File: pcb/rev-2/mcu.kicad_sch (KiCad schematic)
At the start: 8 parts, among them J5 BD125-10-A-0305-0580-L-B, U7 WT02C40C-V3

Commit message: pcb: full rev-2 layout
Mostly finished layout for the rev-2 board
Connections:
- net RAM.MISO: now also U7.A5 (P100); no longer U7.E6 (P010)
- net RAM.MOSI: now also U7.A1 (P006); no longer U7.11 (P009/BUTTON)
- net RAM.SCK: now also U7.A2 (P007); no longer U7.A3 (P008)
- net RAM.~{CS}: now also U7.A6 (P108); no longer JP4.2 (C)
- net SD.MISO: now also U7.E6 (P010); no longer U7.A5 (P100)
- net SD.MOSI: now also U7.11 (P009/BUTTON); no longer U7.A6 (P108)
- net SD.SCK: now also U7.A3 (P008); no longer U7.Z5 (P114)
- net SD.~{CS}: now also JP4.2 (C); no longer U7.Z6 (P115)
- net BUCKEN: now reaches R12.1, U7.B5 (P012)
- net IOVDD_CTRL: now reaches R13.1, U7.C1 (P031)
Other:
- moved on the sheet: R12, R13

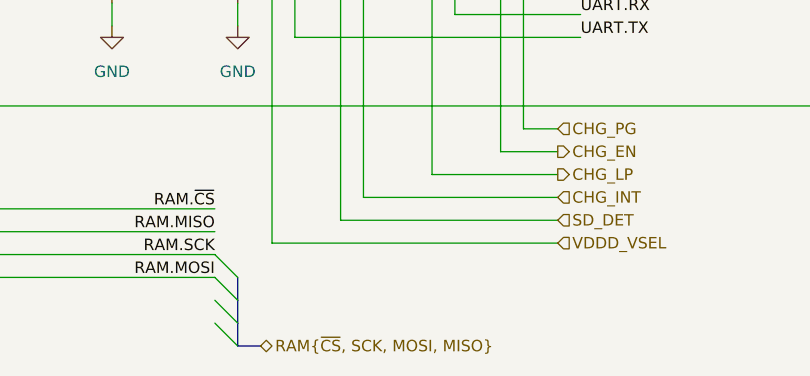
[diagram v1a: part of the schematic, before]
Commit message: pcb: minor schematic cleanup
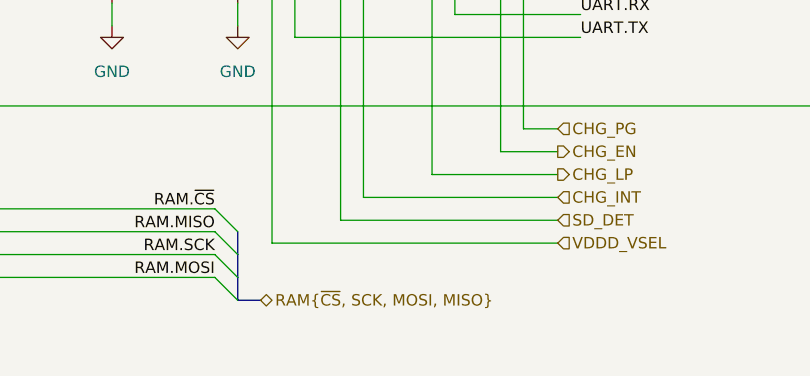
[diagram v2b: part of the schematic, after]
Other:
- title: (none) -> nRF53 Microcontroller

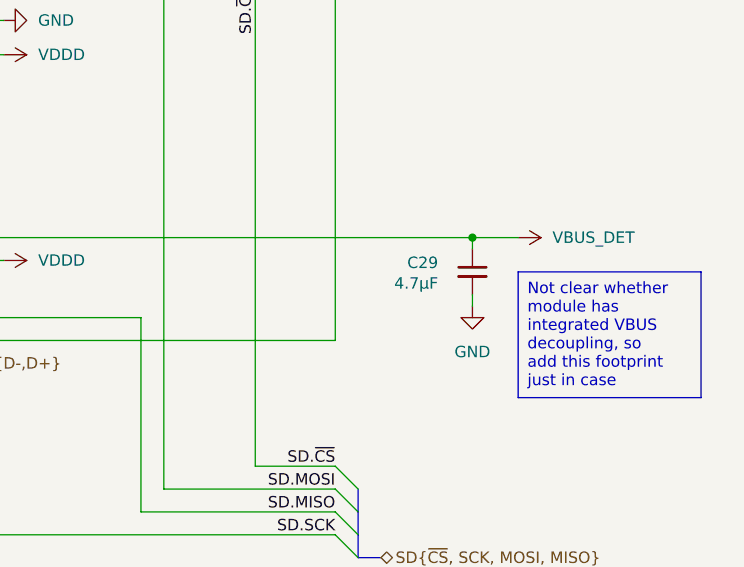
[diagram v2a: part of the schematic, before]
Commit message: pcb: update
Mostly downsize several decoupling capacitors to save space
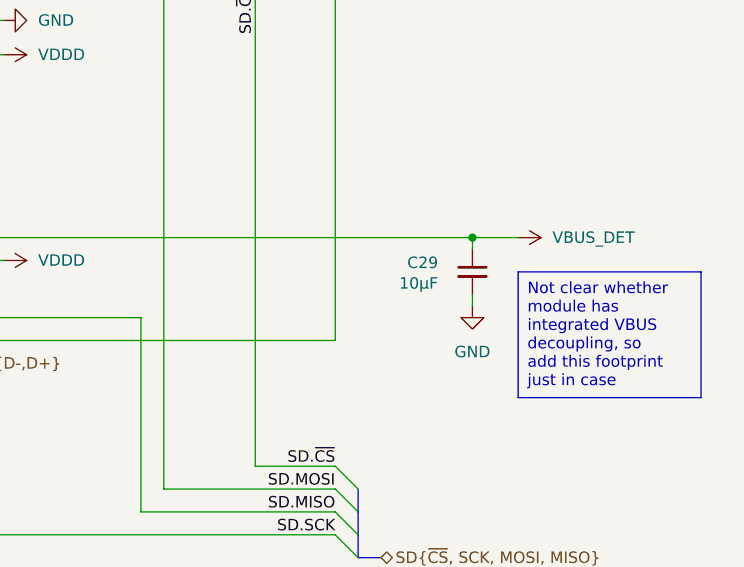
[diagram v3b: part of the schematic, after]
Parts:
- C29: value 4.7µF -> 10µF; footprint Capacitor_SMD:C_0603_1608Metric -> zeus-le:C_0402_1005Metric_Silkscreen_Clearance; manf# C1608X5R1E475K080AC -> CL05A106MP6NUN8
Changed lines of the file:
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@@
 			)
 		)
-		(property "Value" "4.7µF"
+		(property "Value" "10µF"
 			(at 254 110.4899 0)
 			(effects
@@
 			)
 		)
-		(property "Footprint" "Capacitor_SMD:C_0603_1608Metric"
+		(property "Footprint" "zeus-le:C_0402_1005Metric_Silkscreen_Clearance"
 			(at 257.81 109.22 0)
 			(effects
@@
 			)
 		)
-		(property "Description" "Capacitor, decoupling"
+		(property "Description" "Capacitor, decoupling, 10V, X5R"
 			(at 257.81 109.22 0)
 			(effects
@@
 			)
 		)
-		(property "manf#" "C1608X5R1E475K080AC"
+		(property "manf#" "CL05A106MP6NUN8"
 			(at 257.81 109.22 0)
 			(effects

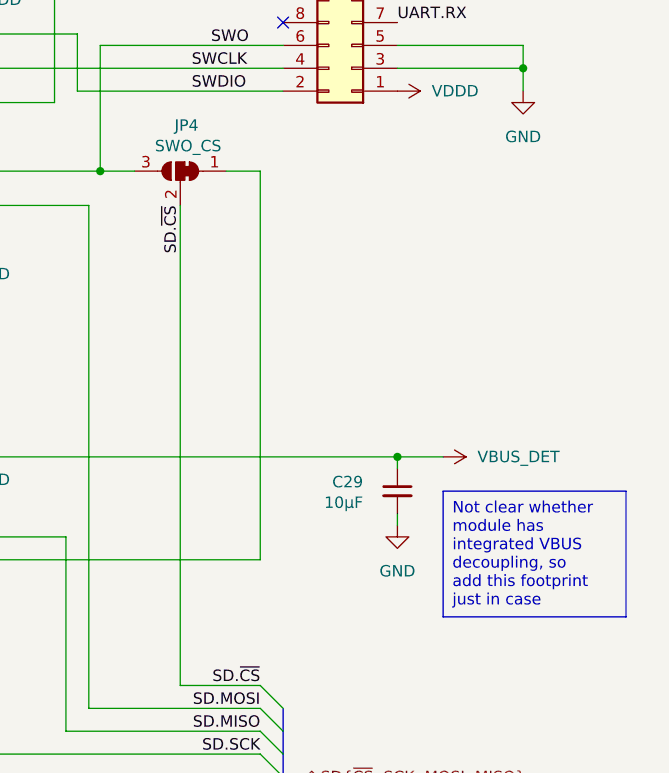
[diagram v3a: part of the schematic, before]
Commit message: pcb: upgrade to KiCad 9.0
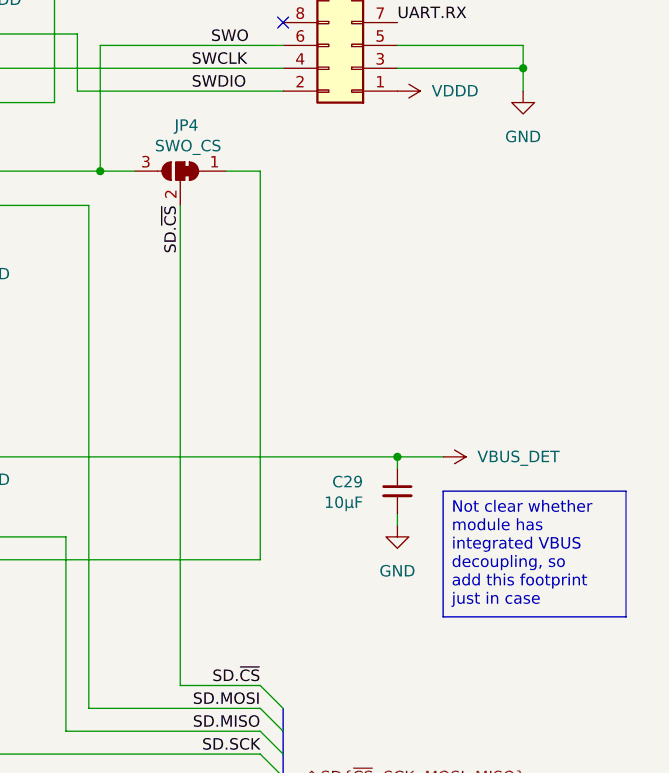
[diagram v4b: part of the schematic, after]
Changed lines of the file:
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@@
 (kicad_sch
-	(version 20231120)
+	(version 20250114)
 	(generator "eeschema")
-	(generator_version "8.0")
+	(generator_version "9.0")
 	(paper "A4")
 	(title_block
@@
 		(rev "2")
 	)
+	(text_box "Not clear whether module has integrated VBUS decoupling, so add this footprint just in case"
+		(exclude_from_sim no)
+		(at 262.89 109.22 0)
+		(size 20.32 13.97)
+		(margins 0.9525 0.9525 0.9525 0.9525)
+		(stroke
+			(width 0)
+			(type default)
+		)
+		(fill
+			(type none)
+		)
+		(effects
+			(font
+				(size 1.27 1.27)
+			)
+			(justify left top)
+		)
+	)
 	(junction
 		(at 60.96 62.23)
@@
 		)
 	)
-	(text_box "Not clear whether module has integrated VBUS decoupling, so add this footprint just in case"
-		(exclude_from_sim no)
-		(at 262.89 109.22 0)
-		(size 20.32 13.97)
-		(stroke
-			(width 0)
-			(type default)
-		)
-		(fill
-			(type none)
-		)
-		(effects
-			(font
-				(size 1.27 1.27)
-			)
-			(justify left top)
-		)
-	)
 	(label "SWO"
 		(at 241.3 59.69 180)
-		(fields_autoplaced yes)
 		(effects
 			(font
@@
 	(label "I2C.SDA"
 		(at 40.64 58.42 0)
-		(fields_autoplaced yes)
 		(effects
 			(font
@@
 	(label "RAM.~{CS}"
 		(at 142.24 149.86 180)
-		(fields_autoplaced yes)
 		(effects
 			(font
@@
 	(label "UART.RX"
 		(at 182.88 128.27 0)
-		(fields_autoplaced yes)
 		(effects
 			(font
@@
 	(label "I2S.WS"
 		(at 71.12 114.3 0)
-		(fields_autoplaced yes)
 		(effects
 			(font
@@
 	(label "UART.TX"
 		(at 182.88 130.81 0)
-		(fields_autoplaced yes)
 		(effects
 			(font
@@
 	(label "RAM.MOSI"
 		(at 142.24 157.48 180)
-		(fields_autoplaced yes)
 		(effects
 			(font
@@
 	(label "BUCKEN"
 		(at 130.81 109.22 270)
-		(fields_autoplaced yes)
 		(effects
 			(font
@@
 	(label "SD.SCK"
 		(at 107.95 105.41 270)
-		(fields_autoplaced yes)
 		(effects
 			(font
@@
 	(label "SWDIO"
 		(at 234.95 64.77 0)
-		(fields_autoplaced yes)
 		(effects
 			(font
@@
 	(label "SD.MISO"
 		(at 242.57 135.89 180)
-		(fields_autoplaced yes)
 		(effects
 			(font
@@
 	(label "SD.~{CS}"
 		(at 242.57 130.81 180)
-		(fields_autoplaced yes)
 		(effects
 			(font
@@
 	(label "RST"
 		(at 237.49 54.61 0)
-		(fields_autoplaced yes)
 		(effects
 			(font
@@
 	(label "I2C.SCL"
 		(at 40.64 62.23 0)
-		(fields_autoplaced yes)
 		(effects
 			(font
@@
 	(label "UART.RX"
 		(at 257.81 57.15 0)
-		(fields_autoplaced yes)
 		(effects
 			(font
@@
 	(label "SD.MOSI"
 		(at 242.57 133.35 180)
-		(fields_autoplaced yes)
 		(effects
 			(font
@@
 	(label "USB.D+"
 		(at 187.96 124.46 0)
-		(fields_autoplaced yes)
 		(effects
 			(font
@@
 	(label "RAM.MISO"
 		(at 142.24 152.4 180)
-		(fields_autoplaced yes)
 		(effects
 			(font
@@
 	(label "RAM.SCK"
 		(at 142.24 154.94 180)
-		(fields_autoplaced yes)
 		(effects
 			(font
@@
 	(label "SD.MOSI"
 		(at 204.47 77.47 0)
-		(fields_autoplaced yes)
 		(effects
 			(font
@@
 	(label "SD.MISO"
 		(at 186.69 104.14 270)
-		(fields_autoplaced yes)
 		(effects
 			(font
@@
 	(label "I2S.SD"
 		(at 71.12 119.38 0)
-		(fields_autoplaced yes)
 		(effects
 			(font
@@
 	(label "SD.SCK"
 		(at 242.57 138.43 180)
-		(fields_autoplaced yes)
 		(effects
 			(font
@@
 	(label "USB.D-"
 		(at 187.96 121.92 0)
-		(fields_autoplaced yes)
 		(effects
 			(font
@@
 	(label "UART.TX"
 		(at 257.81 54.61 0)
-		(fields_autoplaced yes)
 		(effects
 			(font
@@
 	(label "IOVDD_CTRL"
 		(at 144.78 109.22 270)
-		(fields_autoplaced yes)
 		(effects
 			(font
@@
 	(label "I2S.SCK"
 		(at 71.12 116.84 0)
-		(fields_autoplaced yes)
 		(effects
 			(font
@@
 	(label "SWCLK"
 		(at 234.95 62.23 0)
-		(fields_autoplaced yes)
 		(effects
 			(font
@@
 	(label "SD.~{CS}"
 		(at 233.68 77.47 270)
-		(fields_autoplaced yes)
 		(effects
 			(font
@@
 		(shape output)
 		(at 180.34 146.05 0)
-		(fields_autoplaced yes)
 		(effects
 			(font
@@
 		(shape bidirectional)
 		(at 247.65 140.97 0)
-		(fields_autoplaced yes)
 		(effects
 			(font
@@
 		(shape bidirectional)
 		(at 35.56 55.88 180)
-		(fields_autoplaced yes)
 		(effects
 			(font
@@
 		(shape output)
 		(at 68.58 85.09 180)
-		(fields_autoplaced yes)
 		(effects
 			(font
@@
 		(shape output)
 		(at 180.34 143.51 0)
-		(fields_autoplaced yes)
 		(effects
 			(font
@@
 		(shape input)
 		(at 180.34 153.67 0)
-		(fields_autoplaced yes)
 		(effects
 			(font
@@
 		(shape bidirectional)
 		(at 147.32 160.02 0)
-		(fields_autoplaced yes)
 		(effects
 			(font
@@
 		(shape input)
 		(at 180.34 148.59 0)
-		(fields_autoplaced yes)
 		(effects
 			(font
@@
 		(shape input)
 		(at 180.34 140.97 0)
-		(fields_autoplaced yes)
 		(effects
 			(font
@@
 		(shape input)
 		(at 180.34 151.13 0)
-		(fields_autoplaced yes)
 		(effects
 			(font
@@
 		(shape bidirectional)
 		(at 199.39 119.38 0)
-		(fields_autoplaced yes)
 		(effects
 			(font
@@
 		(shape input)
 		(at 66.04 111.76 180)
-		(fields_autoplaced yes)
 		(effects
 			(font
@@
 		(shape input)
 		(at 80.01 110.49 180)
-		(fields_autoplaced yes)
-		(effects
-			(font
+		(effects
+			(font

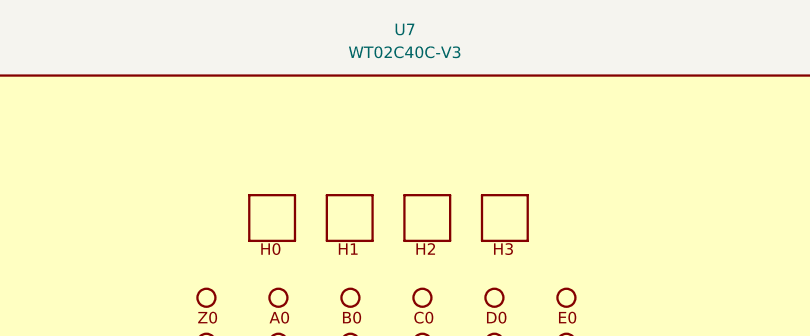
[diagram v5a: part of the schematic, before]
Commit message: Update PCBs
* Update to KiCad 10
* Update footprint for nRF53 module based on 1.01 datasheet with
  actually readable mechanical drawing
* Add 3D model for production nRF53 module
* Remove overlapping silkscreen on rev-1 with production nRF53 module
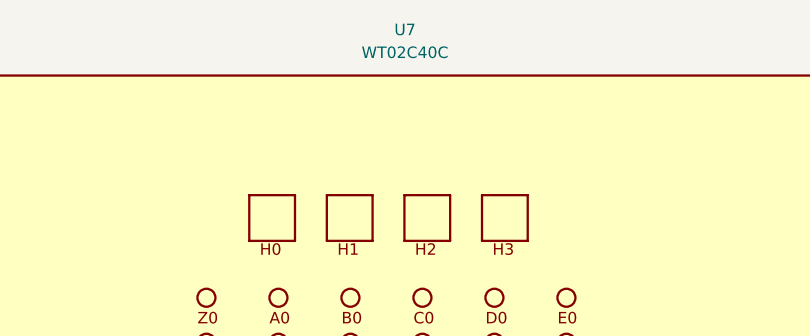
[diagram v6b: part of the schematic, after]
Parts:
- U7: value WT02C40C-V3 -> WT02C40C; footprint zeus-le:WT02C40C -> zeus-le:WT02C40C-VC; symbol zeus-le:WT02V40V -> zeus-le:WT02C40C; digikey# (none) -> 1914-WT02C40CCT-ND; manf# WT02C40C-V3 -> WT02C40C
